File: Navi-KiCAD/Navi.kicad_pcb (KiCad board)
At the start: 4 copper layers, 50.8 x 40 mm, 216 parts, among them J1 0734120110, J2 0734120110, J3 0734120110, J4 473460001, J5 AXK5S80047YG, J6 AXK5S80047YG, Q1 IRLML5203TRPBF, Q2 IRLML5203TRPBF, U1 LP55231SQE/NOPB, U10 TPS54232DR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

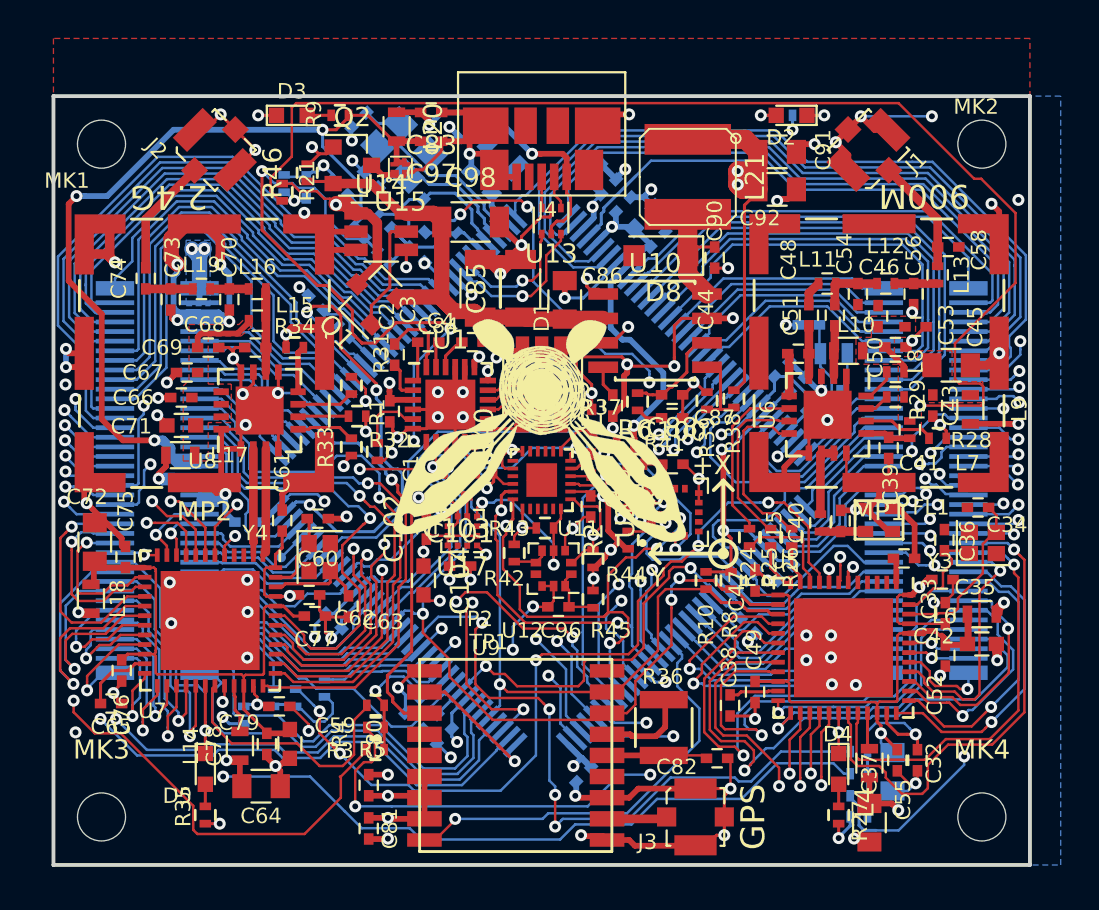
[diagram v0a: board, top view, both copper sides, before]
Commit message: Cleaned up silkscreen.
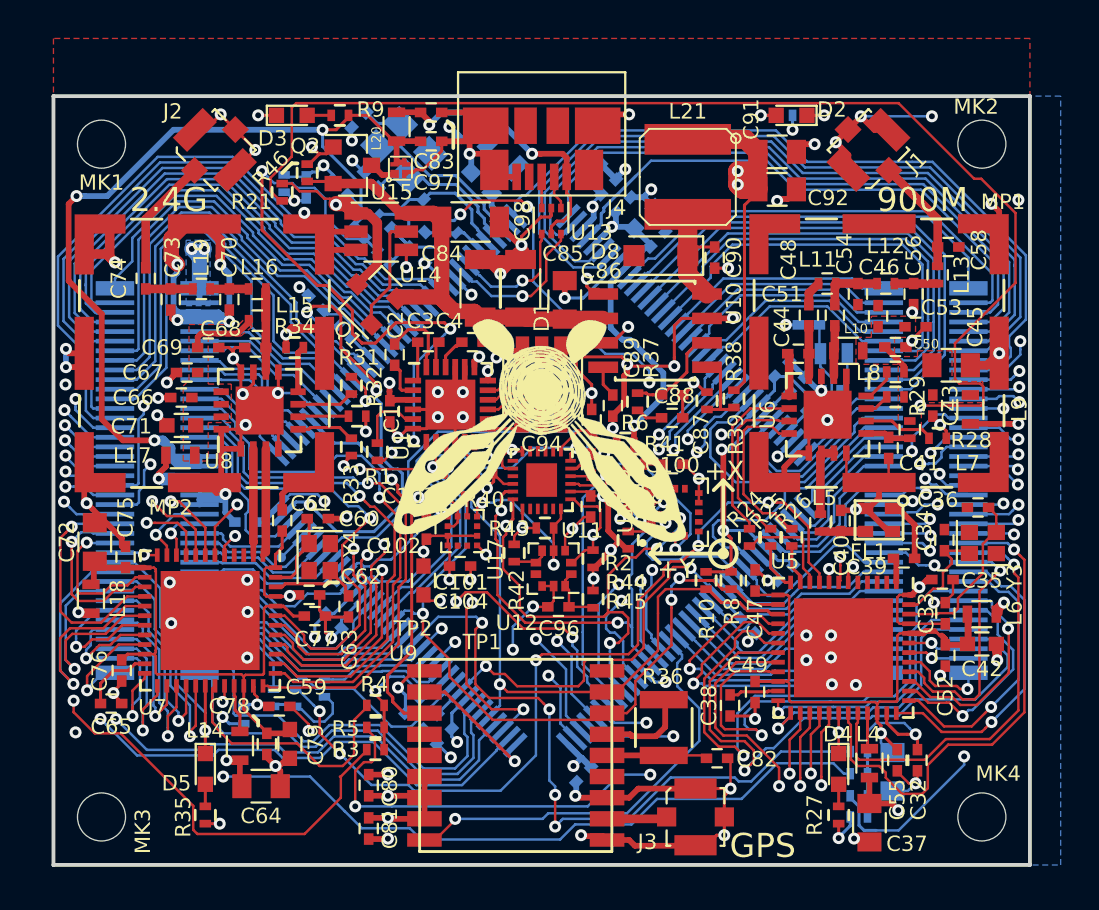
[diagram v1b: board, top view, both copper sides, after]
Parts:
- U16: value LSM6DS33 -> LSM6DS33TR
- U17: value LSM303AH -> LSM303AHTR
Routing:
- net /Connectors/2.4-DIO-20: track 15.6 -> 15.0 mm
- net /Connectors/PD16: track 22.1 -> 21.5 mm
